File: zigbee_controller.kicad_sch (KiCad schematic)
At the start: 80 parts, among them J1 KF635, J10 TerminalBlock_KF301-5.0, J11 TerminalBlock_KF301-5.0, J12 TerminalBlock_KF301-5.0, J13 TerminalBlock_KF301-5.0, J3 Conn_01x06, J4 Conn_01x07, J5 Conn_01x05, P1 USB_C_Receptacle_GCT_USB4105, Q2 IRLB3813, Q3 IRLB3813, Q4 IRLB3813, Q5 IRLB3813, SW2 EN, SW4 Boot, U1 TPS54560, U2 ESP32-C6-MINI-1, U4 TC4427, U5 TC4427, U6 RT9080, U9 CH224K

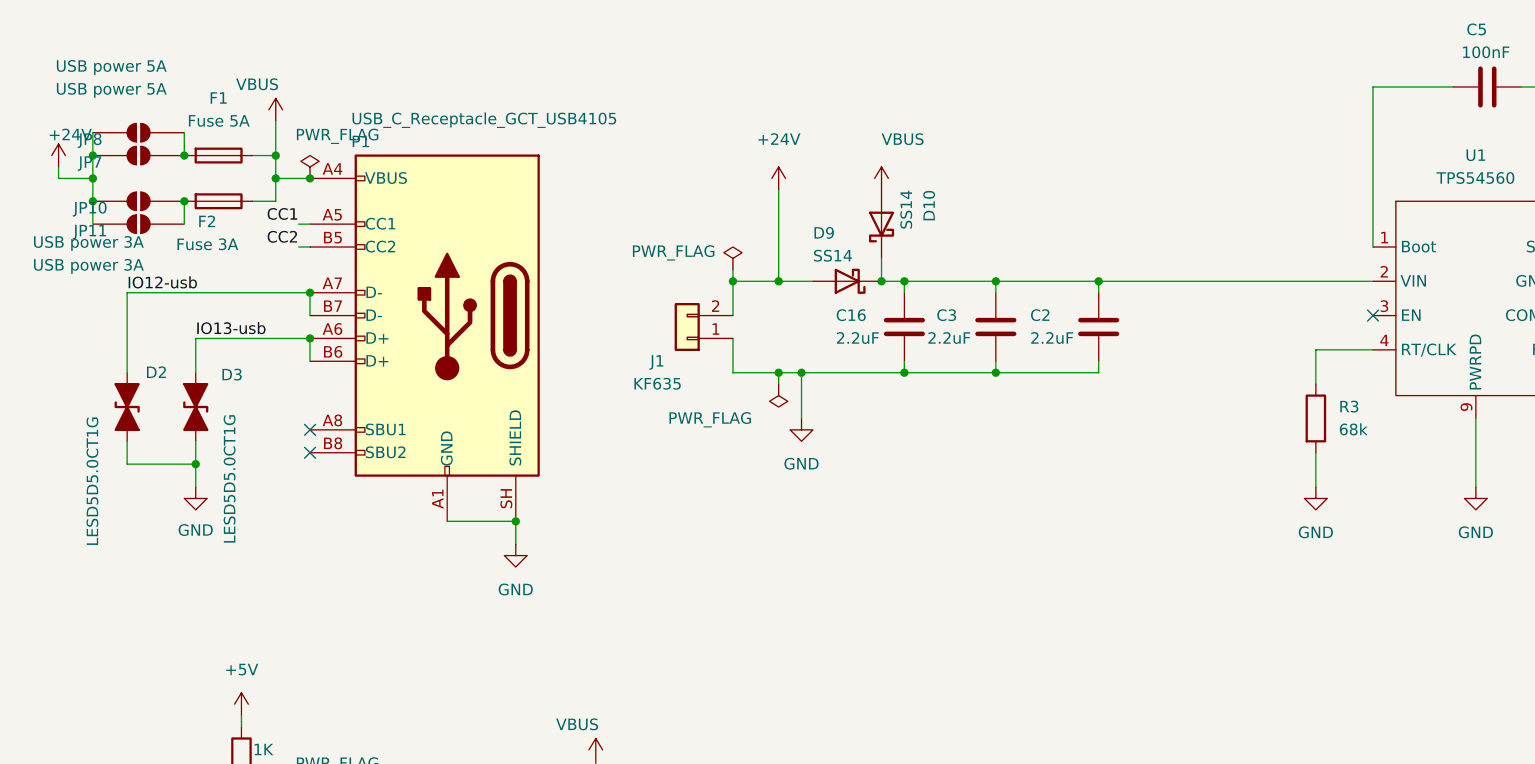
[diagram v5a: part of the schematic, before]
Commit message: Optimize VBUS vias
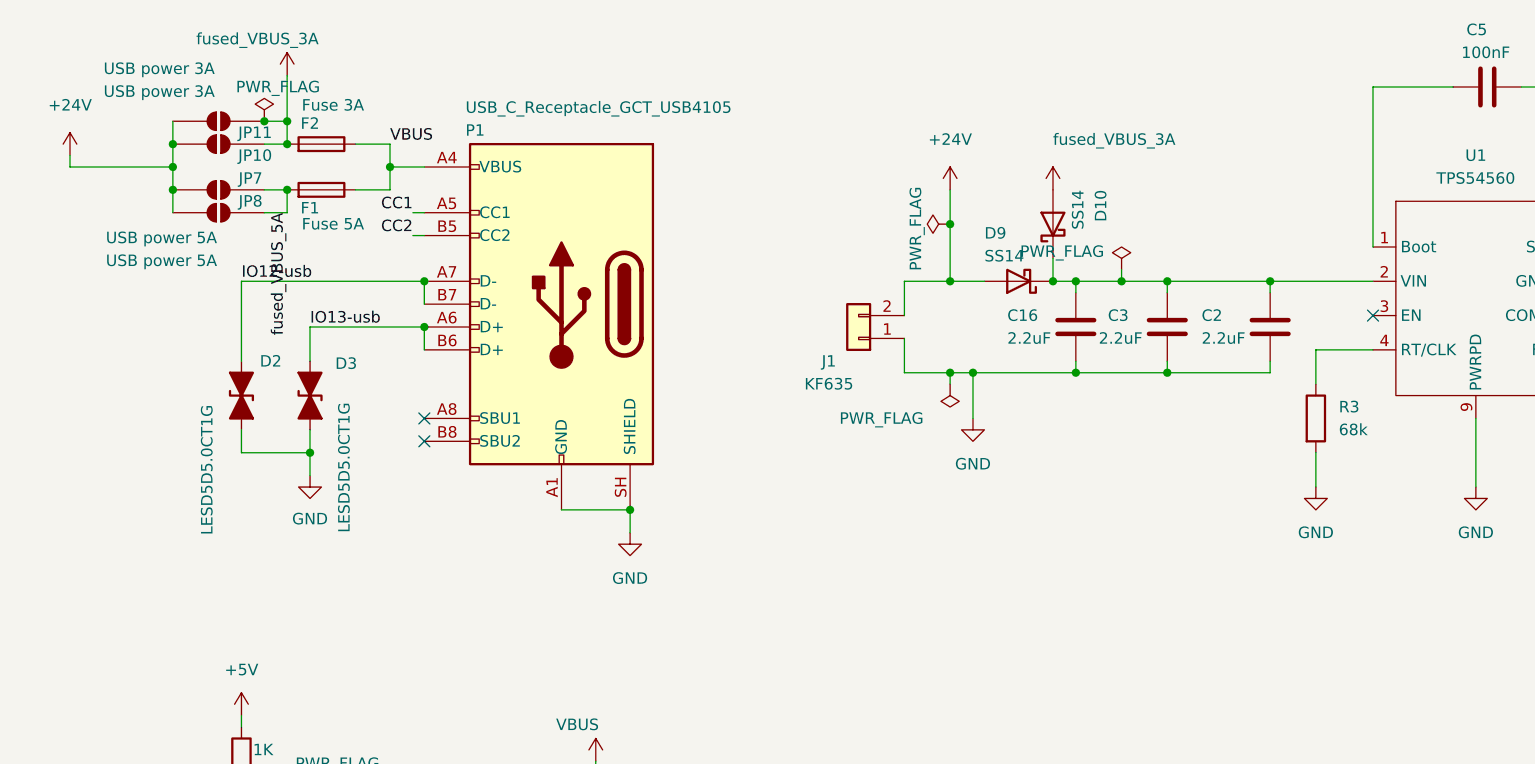
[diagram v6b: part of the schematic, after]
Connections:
- net VBUS: no longer D10.2 (A)
- net fused_VBUS_3A: now reaches F2.2, JP10.2 (B), JP11.2 (B)
- net fused_VBUS_3A: now also D10.2 (A)
- net fused_VBUS_5A: now reaches F1.2, JP7.2 (B), JP8.2 (B)
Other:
- moved on the sheet: C16, C2, C3, D10, D2, D3, D9, F2, J1, JP10, JP11, P1

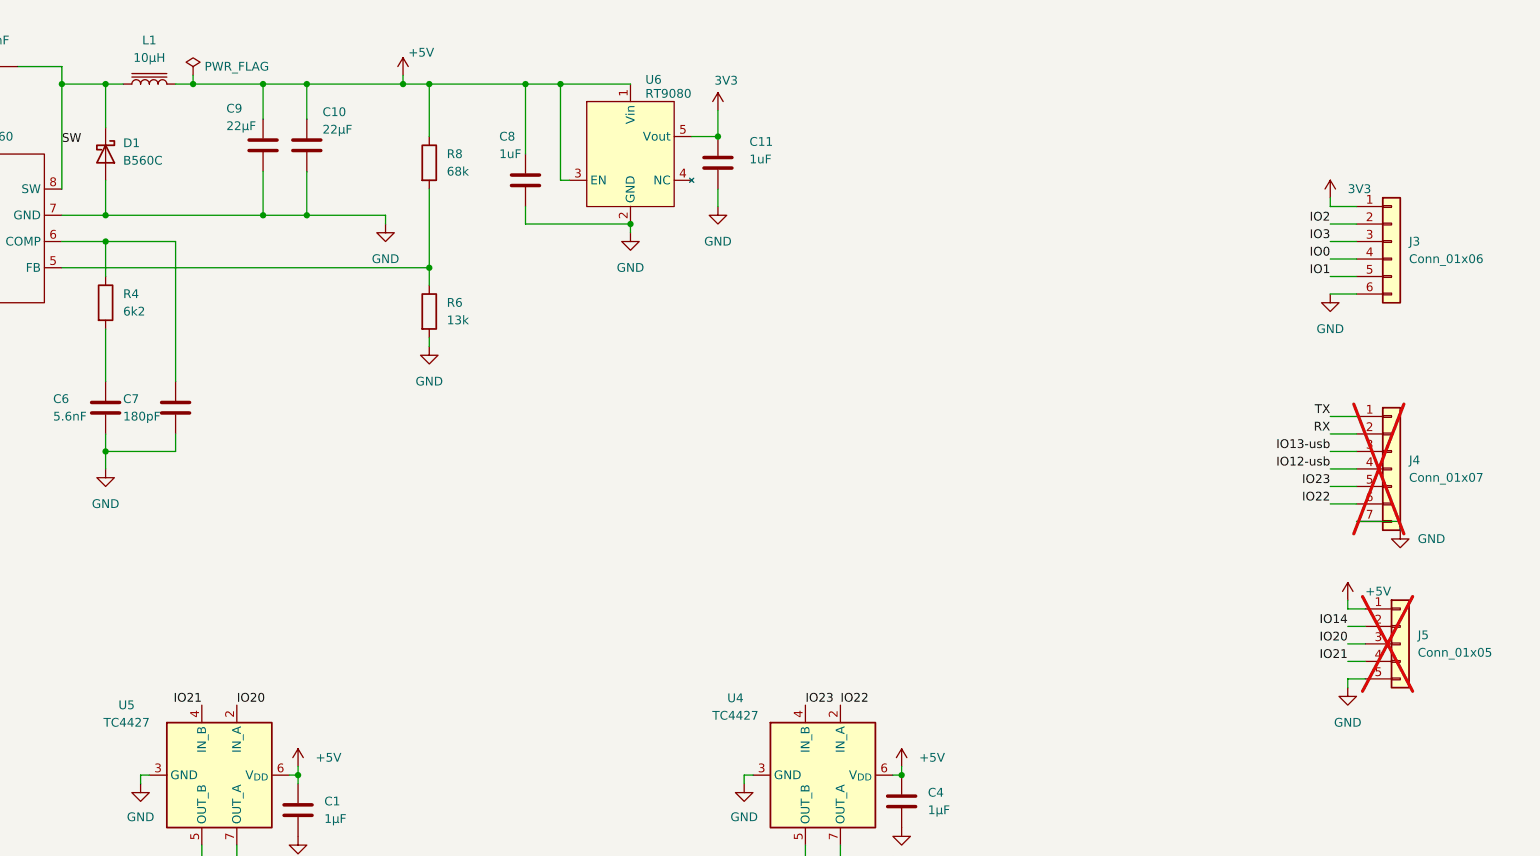
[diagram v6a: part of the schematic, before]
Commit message: Add pulldown resistors between ESP32 and TC4427
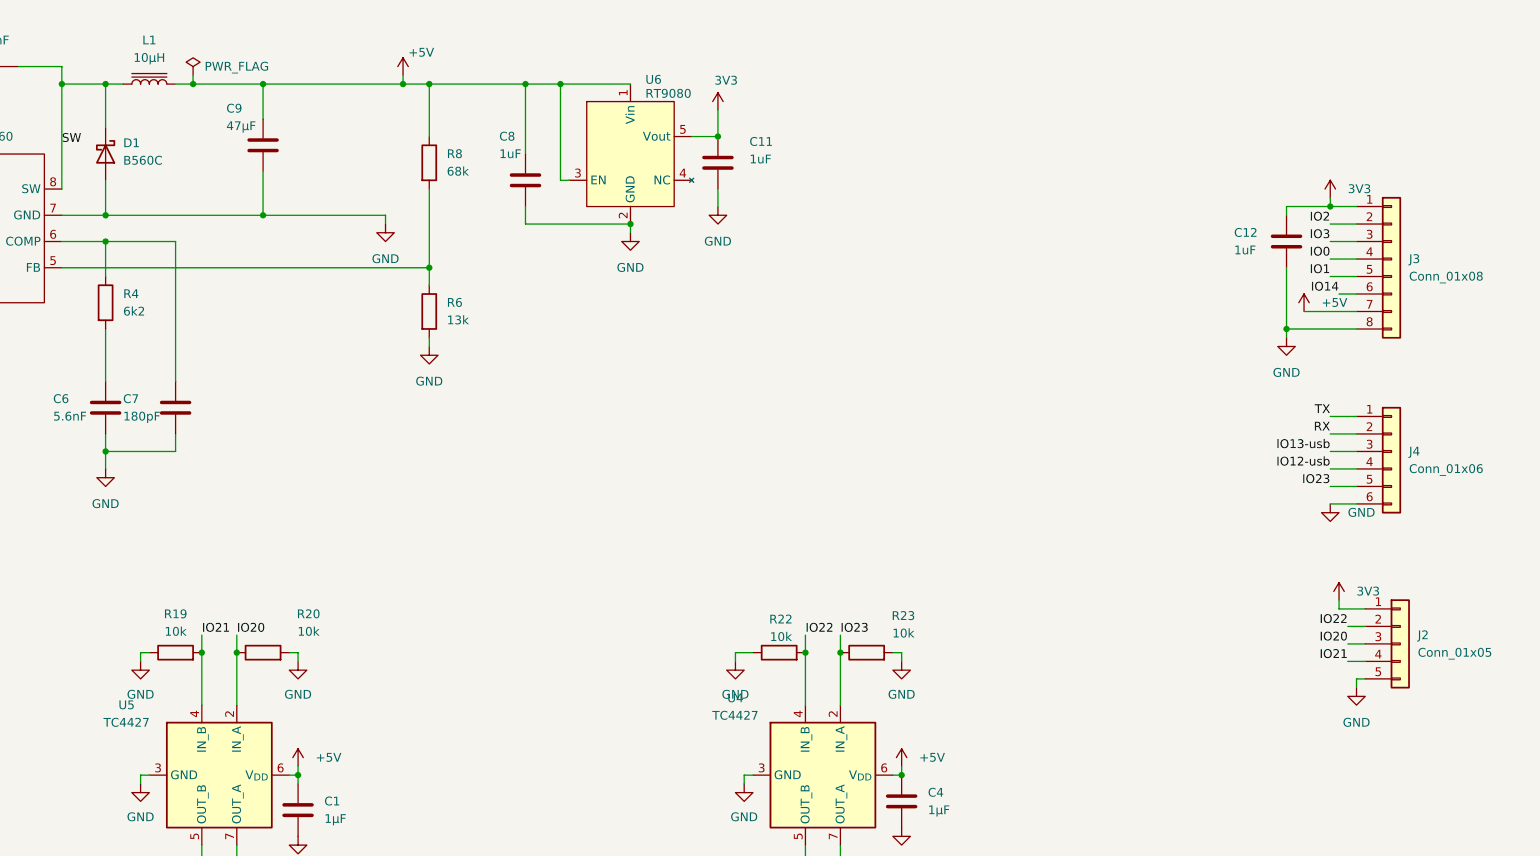
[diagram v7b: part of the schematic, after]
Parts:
- removed C10: 22μF, Capacitor_SMD:C_1206_3216Metric, symbol Device:C
- removed J3: Conn_01x06, Connector_JST:JST_XH_B6B-XH-A_1x06_P2.50mm_Vertical, symbol Connector_Generic:Conn_01x06
- removed J4: Conn_01x07, Connector_JST:JST_XH_B7B-XH-A_1x07_P2.50mm_Vertical, symbol Connector_Generic:Conn_01x07
- removed J5: Conn_01x05, Connector_JST:JST_XH_B5B-XH-A_1x05_P2.50mm_Vertical, symbol Connector_Generic:Conn_01x05
- added C12: 1uF, Capacitor_SMD:C_1206_3216Metric, symbol Device:C
- added J2: Conn_01x05, Connector_JST:JST_XH_B5B-XH-A_1x05_P2.50mm_Vertical, symbol Connector_Generic:Conn_01x05
- added J3: Conn_01x08, Connector_JST:JST_XH_B8B-XH-A_1x08_P2.50mm_Vertical, symbol Connector_Generic:Conn_01x08
- added J4: Conn_01x06, Connector_JST:JST_XH_B6B-XH-A_1x06_P2.50mm_Vertical, symbol Connector_Generic:Conn_01x06
- added R19, R20, R22, R23: 10k, Resistor_SMD:R_1206_3216Metric, symbol Device:R
- C9: value 22μF -> 47μF
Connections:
- net +5V: now also J3.7 (Pin_7)
- net 3V3: now also C12.1, J2.1 (Pin_1), J3.1 (Pin_1)
- net GND: now also C12.2, J2.5 (Pin_5), J3.8 (Pin_8), J4.6 (Pin_6), R19.1, R20.2, R22.1, R23.2
- net IO0: now also J3.4 (Pin_4)
- net IO1: now also J3.5 (Pin_5)
- net IO12-usb: now also J4.4 (Pin_4)
- net IO13-usb: now also J4.3 (Pin_3)
- net IO14: now also J3.6 (Pin_6)
- net IO2: now also J3.2 (Pin_2)
- net IO20: now also J2.3 (Pin_3), R20.1
- net IO21: now also J2.4 (Pin_4), R19.2
- net IO22: now also U4.4 (IN_B), J2.2 (Pin_2), R22.2; no longer U4.2 (IN_A)
- net IO23: now also U4.2 (IN_A), J4.5 (Pin_5), R23.1; no longer U4.4 (IN_B)
- net IO3: now also J3.3 (Pin_3)
- net RX: now also J4.2 (Pin_2)
- net TX: now also J4.1 (Pin_1)

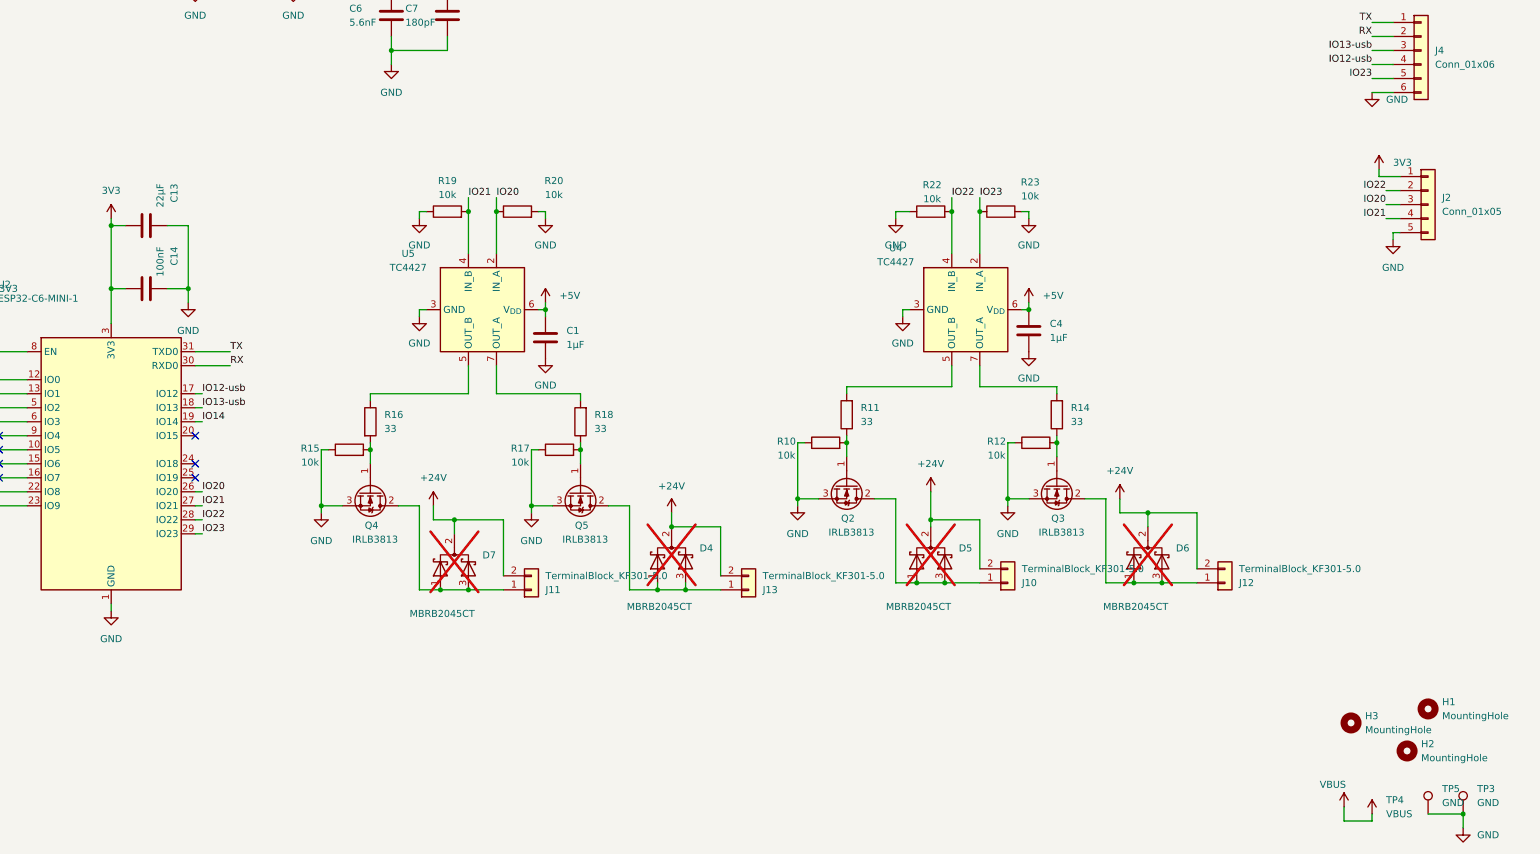
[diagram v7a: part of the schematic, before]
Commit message: Add extra capacitor to avoid brownout
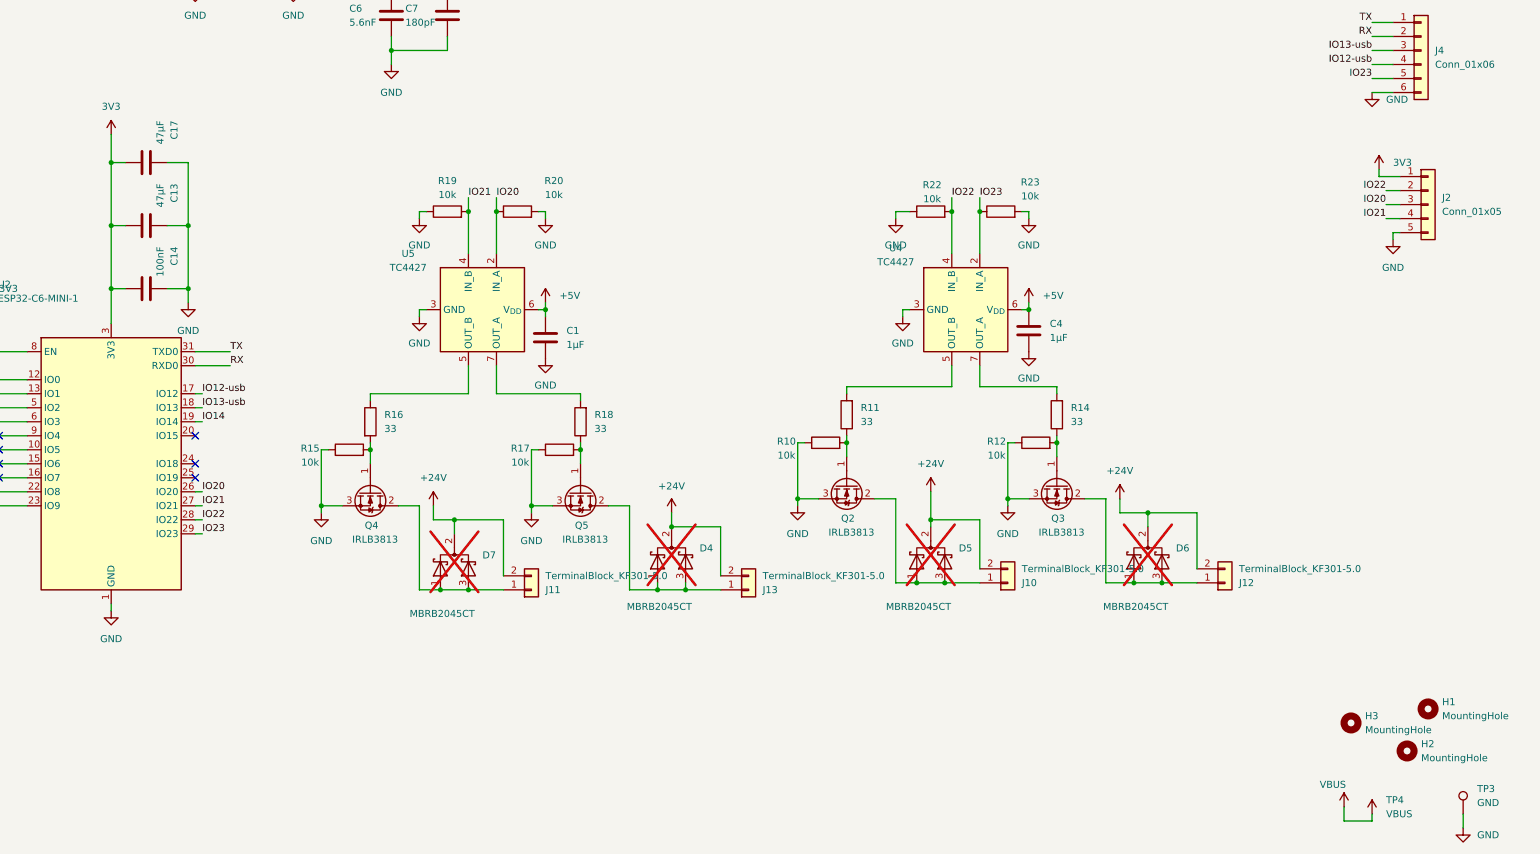
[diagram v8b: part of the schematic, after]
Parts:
- removed TP5: GND, TestPoint:TestPoint_Pad_D2.0mm, symbol Connector:TestPoint
- added C17: 47μF, Capacitor_SMD:C_1206_3216Metric, symbol Device:C
- C13: value 22μF -> 47μF
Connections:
- net 3V3: now also C17.2
- net GND: now also C17.1
